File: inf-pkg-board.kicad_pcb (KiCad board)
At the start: 4 copper layers, 68.6 x 53.3 mm, 60 parts, among them J1 stemmaQT, J2 Conn_01x01_Pin, J3 Conn_01x01_Pin, J4 SWD, J5 USB_C_Receptacle_USB2.0_14P, J6 ePaper Hat, Q1 2N7002, U1 ME6211C33M5, U2 W25Q128JVS, U3 RP2040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

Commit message: fixes
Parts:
- removed U1: ME6211C33M5, Package_TO_SOT_SMD:SOT-23-5
- added C22: 100n, Capacitor_SMD:C_0402_1005Metric, F.Cu at (118.4, 96.3)
- added C23: 100p, Capacitor_SMD:C_0402_1005Metric, F.Cu at (83.8, 105.2)
- added C24: 100p, Capacitor_SMD:C_0402_1005Metric, F.Cu at (77.4, 98.8)
- added D2: LED, Diode_SMD:D_0805_2012Metric, F.Cu at (93.9, 97.8)
- added D3: LED, Diode_SMD:D_0805_2012Metric, F.Cu at (97.5, 99.6)
- added G***: LOGO, Symbol:infinity-small, F.Cu at (94.2, 117.9)
- added J7: Conn_01x01_Pin, Connector_PinHeader_1.00mm:PinHeader_1x01_P1.00mm_Vertical, F.Cu at (82.0, 112.0)
- added J8: Conn_01x01_Pin, Connector_PinHeader_1.00mm:PinHeader_1x01_P1.00mm_Vertical, F.Cu at (82.0, 109.0)
- added JP4: Jumper_2_Small_Bridged, Jumper:SolderJumper-2_P1.3mm_Bridged_Pad1.0x1.5mm, F.Cu at (138.0, 82.3)
- added Q2: AO3400A, Package_TO_SOT_SMD:SOT-23, F.Cu at (126.7, 112.6)
- added R14: 330, Resistor_SMD:R_0402_1005Metric, F.Cu at (136.4, 102.1)
- added R15: 5.1k, Resistor_SMD:R_0402_1005Metric, F.Cu at (85.6, 98.3)
- added R16: 330, Resistor_SMD:R_0402_1005Metric, F.Cu at (94.7, 99.3)
- added R17: 330, Resistor_SMD:R_0402_1005Metric, F.Cu at (92.1, 99.8)
- added R2: 27, Resistor_SMD:R_0402_1005Metric, F.Cu at (111.3, 120.7)
- added REF**: OSHW-Symbol_6.7x6mm_SilkScreen, Symbol:OSHW-Symbol_6.7x6mm_SilkScreen, F.Cu at (131.4, 82.3)
- added U7: SPX3819M5-L-3-3, Package_TO_SOT_SMD:SOT-23-5, F.Cu at (120.8, 98.7)
- L1: footprint Inductor_SMD:L_0201_0603Metric -> Inductor_SMD:L_0402_1005Metric
- Q1: value 2N7002 -> AO3400A
- R1, R13, R5, R6: footprint Capacitor_SMD:C_0402_1005Metric -> Resistor_SMD:R_0402_1005Metric
- R12: value 10k -> 1M; footprint Resistor_SMD:R_0805_2012Metric -> Resistor_SMD:R_0402_1005Metric
- R4: footprint Resistor_SMD:R_0402_1005Metric -> Resistor_SMD:R_0805_2012Metric
- moved C21 42.3 mm to (119.6, 101.9), turned to 90 degrees
- moved R12 24.7 mm to (116.1, 116.4), turned to -90 degrees
- moved R4 6.28 mm to (113.2, 101.2), turned to 90 degrees
- moved J3 2.55 mm to (85.9, 104.9)
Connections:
- C20 pad 2: Net-(U4-VBACKUP) -> Net-(Q2-G)
- R12 pad 1: Net-(D1-K) -> Net-(Q2-G)
- R12 pad 2: GND -> Net-(Q2-S)
- U3 pad 13: unconnected-(U3-GPIO10-Pad13) -> Net-(D2-A)
- U3 pad 14: unconnected-(U3-GPIO11-Pad14) -> Net-(D3-A)
- U3 pad 17: unconnected-(U3-GPIO14-Pad17) -> Net-(J8-Pin_1)
- U3 pad 18: unconnected-(U3-GPIO15-Pad18) -> Net-(J7-Pin_1)
- U4 pad 1: /32kHz -> Net-(U4-CLKOUT)
- U4 pad 2: /CC_GND -> Net-(Q2-S)
- U4 pad 6: Net-(U4-VBACKUP) -> Net-(Q2-G)
- U5 pad 2: Net-(J3-Pin_1) -> Net-(U5-FMI)
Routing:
- net Net-(Q2-G): track 0.00 -> 40.8 mm, vias 0 -> 3
- net Net-(U4-VBACKUP): track 35.1 -> 0.00 mm, vias 3 -> 0
- net Net-(J8-Pin_1): track 0.00 -> 30.4 mm, vias 0 -> 2
- net Net-(J7-Pin_1): track 0.00 -> 29.9 mm, vias 0 -> 2
- net GND: track 84.3 -> 101.8 mm, vias 38 -> 42
- net Net-(Q2-S): track 0.00 -> 17.5 mm, vias 0 -> 2
- net /CC_GND: track 79.0 -> 70.1 mm, vias 5 -> 4
- net Net-(D2-A): track 0.00 -> 4.26 mm
- net Net-(U5-FMI): track 0.00 -> 3.63 mm
- net Net-(D3-A): track 0.00 -> 2.88 mm
- net Net-(U5-~{SEN}): track 3.88 -> 6.64 mm
- net +3V3: track 75.6 -> 78.3 mm
- net /INIT: track 49.9 -> 47.4 mm
- net /32kHz: track 55.9 -> 53.5 mm
- net /D/C: track 34.0 -> 31.7 mm
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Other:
- board text added: "cut me"

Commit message: fix bom error / add debug pads
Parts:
- added J9: Conn_ARM_SWD_TagConnect_TC2030, Connector:Tag-Connect_TC2030-IDC-FP_2x03_P1.27mm_Vertical, F.Cu at (115.5, 90.9)
- added TP_CC_LATCH1: TestPoint, TestPoint:TestPoint_Pad_D1.5mm, F.Cu at (116.7, 80.3)
- added TP_CLK1: TestPoint, TestPoint:TestPoint_Pad_D1.5mm, F.Cu at (106.9, 116.0)
- added TP_GND1: TestPoint, TestPoint:TestPoint_Pad_D1.5mm, F.Cu at (130.8, 120.8)
- added TP_INT1: TestPoint, TestPoint:TestPoint_Pad_D1.5mm, F.Cu at (113.9, 122.8)
- added TP_V33: 3.3V_TEST, TestPoint:TestPoint_Pad_D2.0mm, F.Cu at (118.5, 121.3)
- added TP_VB1: VBUS_TEST, TestPoint:TestPoint_Pad_D2.0mm, F.Cu at (140.3, 87.1)
- J4: footprint Connector_PinHeader_1.27mm:PinHeader_2x05_P1.27mm_Vertical -> Connector_PinHeader_1.27mm:PinHeader_2x05_P1.27mm_Vertical_SMD
- R3: footprint Capacitor_SMD:C_0402_1005Metric -> Resistor_SMD:R_0402_1005Metric
- moved J4 27.3 mm to (137.9, 80.9)
- moved JP4 7.99 mm to (133.2, 75.9)
- moved REF** 1.80 mm to (130.1, 81.1)
- moved C10 1.42 mm to (106.2, 88.8)
- moved G*** 0.87 mm to (93.4, 117.6)
- moved C8 0.62 mm to (105.2, 88.0)
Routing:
- net /SWD: track 12.8 -> 50.7 mm, vias 0 -> 2
- net /SWCLK: track 17.6 -> 51.5 mm, vias 2 -> 6
- net /RUN: track 58.0 -> 85.7 mm, vias 3 -> 6
- net GND: track 101.8 -> 121.8 mm, vias 42 -> 45
- net +3V3: track 78.3 -> 94.5 mm, vias 12 -> 15
- net VBUS: track 35.9 -> 48.2 mm
- net /CC_GND: track 70.1 -> 63.7 mm
- net Net-(Q2-S): track 17.5 -> 23.0 mm
- net /32kHz: track 53.5 -> 58.6 mm
- net Net-(Q1-G): track 30.2 -> 31.9 mm
- net +1V1: track 29.0 -> 28.4 mm
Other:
- board text added: "return to sender"
- board text added: "rev2"

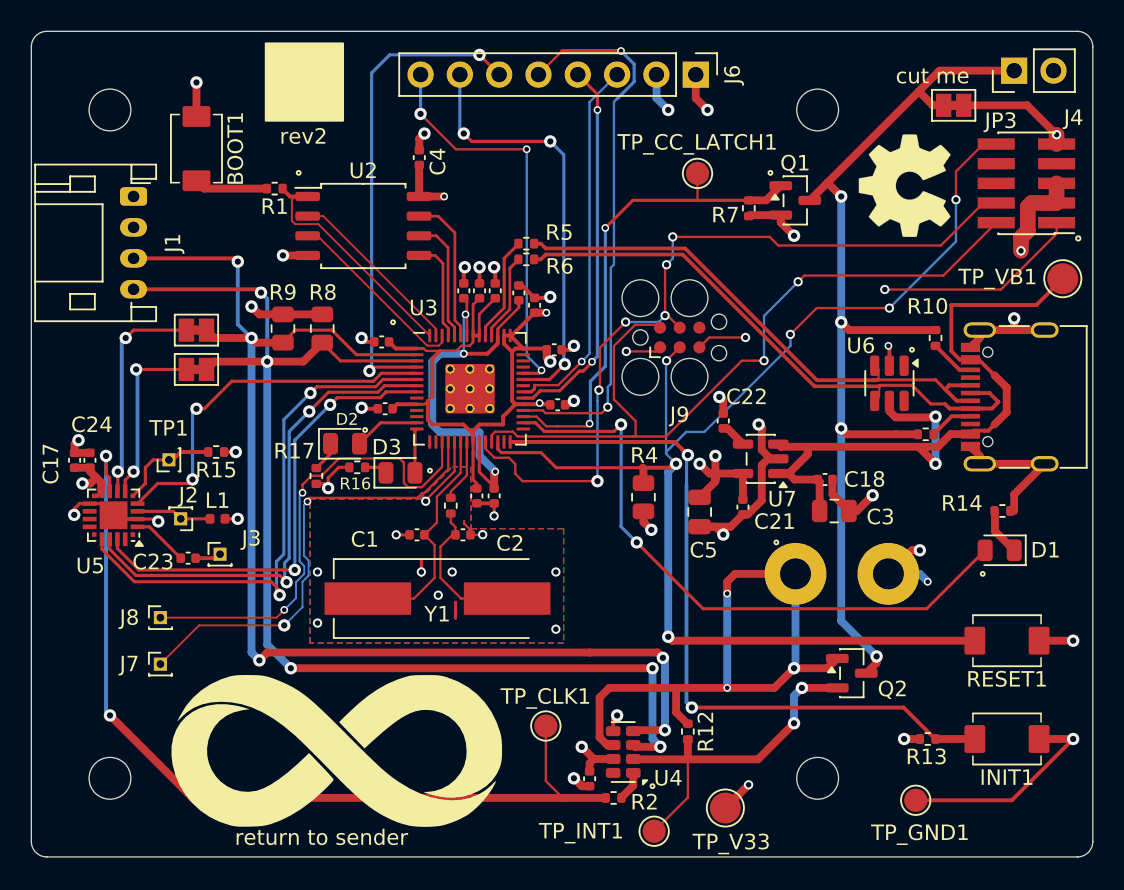
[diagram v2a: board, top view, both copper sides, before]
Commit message: bom optimization
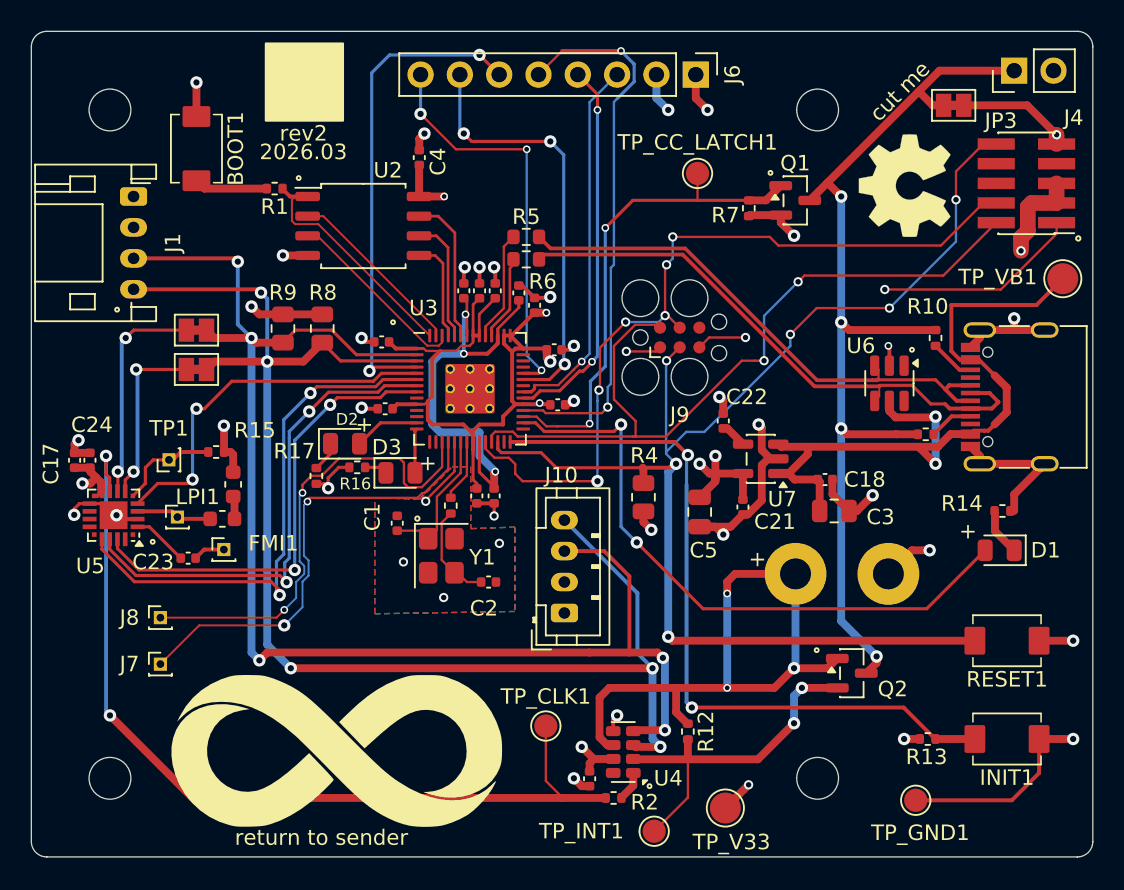
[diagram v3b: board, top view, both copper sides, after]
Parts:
- removed J2, J3: Conn_01x01_Pin, Connector_PinHeader_1.00mm:PinHeader_1x01_P1.00mm_Vertical
- added FMI1: Conn_01x01_Pin, Connector_PinHeader_1.00mm:PinHeader_1x01_P1.00mm_Vertical, F.Cu at (86.1, 104.6)
- added J10: stemmaQT, Connector_JST:JST_PH_B4B-PH-K_1x04_P2.00mm_Vertical, F.Cu at (108.1, 108.7)
- added L2: 68nH, Inductor_SMD:L_0603_1608Metric, F.Cu at (86.7, 100.4)
- added LPI1: Conn_01x01_Pin, Connector_PinHeader_1.00mm:PinHeader_1x01_P1.00mm_Vertical, F.Cu at (83.1, 102.5)
- C1, C2: value 27p -> 33p
- L1: value 120nH -> 68nH; footprint Inductor_SMD:L_0402_1005Metric -> Inductor_SMD:L_0603_1608Metric
- R5, R6: footprint Resistor_SMD:R_0402_1005Metric -> Resistor_SMD:R_0603_1608Metric
- Y1: value ABLS-12.000MHZ-B4-T -> Crystal_GND2; footprint RP2040_minimal:Crystal_SMD_HC49-US -> Crystal:Crystal_SMD_3225-4Pin_3.2x2.5mm
- moved C2 3.47 mm to (103.2, 106.7)
- moved Y1 2.78 mm to (100.2, 105.0), turned to -90 degrees
- moved C1 1.48 mm to (97.3, 102.9), turned to 90 degrees
- moved R5 0.44 mm to (105.6, 84.4)
- moved L1 0.31 mm to (86.0, 102.6)
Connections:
- L1 pad 2: GND -> Net-(L1-Pad2)
- Y1 pad 2: Net-(C2-Pad1) -> GND
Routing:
- net /SCL: track 78.6 -> 90.6 mm
- net /SDA: track 81.3 -> 91.1 mm
- net GND: track 121.8 -> 114.6 mm, vias 45 -> 37
- net /XIN: track 14.9 -> 9.34 mm
- net Net-(C2-Pad1): track 9.69 -> 6.38 mm
- net Net-(L1-Pad2): track 0.00 -> 1.48 mm
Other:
- board text added: "+"
- board text added: "2026.03"

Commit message: more ground
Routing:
- net +3V3: track 94.3 -> 97.3 mm, vias 15 -> 18
- net GND: track 114.6 -> 117.6 mm, vias 37 -> 39
- net +1V1: track 28.4 -> 27.4 mm
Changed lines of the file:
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@@
 		(tags "capacitor")
 		(property "Reference" "C2"
-			(at -0.3 1.7 0)
+			(at 0 1.3 0)
 			(layer "F.SilkS")
 			(effects
@@
 		(tags "capacitor")
 		(property "Reference" "C1"
-			(at 0.4 -1.6 90)
+			(at 0.4 -1.6 180)
 			(layer "F.SilkS")
 			(effects
@@
 		(tags "Through hole pin header THT 1x01 1.00mm single row")
 		(property "Reference" "LPI1"
-			(at 1.3 -1.3 0)
+			(at 0.2 -1.6 0)
 			(layer "F.SilkS")
 			(effects
@@
 	)
 	(segment
+		(start 101.6 87.404)
+		(end 103.632 87.404)
+		(width 0.254)
+		(layer "F.Cu")
+		(net 1)
+	)
+	(segment
 		(start 138.77 119.04)
 		(end 138.77 116.84)
@@
 	)
 	(segment
+		(start 102.441 102.341)
+		(end 102.6 102.5)
+		(width 0.2032)
+		(layer "F.Cu")
+		(net 1)
+	)
+	(segment
 		(start 105.156 87.54)
 		(end 105.372 87.54)
@@
 	)
 	(segment
+		(start 102.441 101.615)
+		(end 102.441 102.341)
+		(width 0.2032)
+		(layer "F.Cu")
+		(net 1)
+	)
+	(segment
 		(start 116.84 103.124)
 		(end 118.844 103.124)
@@
 	)
 	(via
+		(at 96 103.6)
+		(size 0.8)
+		(drill 0.4)
+		(layers "F.Cu" "B.Cu")
+		(free yes)
+		(net 1)
+	)
+	(via
 		(at 128.016 101.092)
 		(size 0.8)
@@
 	)
 	(via
+		(at 102.6 102.5)
+		(size 0.8)
+		(drill 0.4)
+		(layers "F.Cu" "B.Cu")
+		(net 1)
+	)
+	(via
 		(at 101.665 86.36)
 		(size 0.8)
@@
 	)
 	(segment
+		(start 96.774 91.186)
+		(end 96.774 90.574)
+		(width 0.254)
+		(layer "F.Cu")
+		(net 5)
+	)
+	(segment
 		(start 104.2 91.303252)
 		(end 104.722 91.825252)
@@
 	)
 	(segment
+		(start 102.199 100.0945)
+		(end 102.199 99.7)
+		(width 0.2)
+		(layer "F.Cu")
+		(net 5)
+	)
+	(segment
 		(start 101.572748 96.52)
 		(end 102.094374 97.041626)
@@
 	)
 	(segment
+		(start 103.30613 89.00613)
+		(end 103.25813 89.00613)
+		(width 0.254)
+		(layer "F.Cu")
+		(net 5)
+	)
+	(segment
+		(start 103.00613 89.00613)
+		(end 103.30613 89.00613)
+		(width 0.254)
+		(layer "F.Cu")
+		(net 5)
+	)
+	(segment
 		(start 99.06 95.2125)
 		(end 99.2765 94.996)
@@
 	)
 	(segment
+		(start 102.6 89.396)
+		(end 102.998 88.998)
+		(width 0.1778)
+		(layer "F.Cu")
+		(net 5)
+	)
+	(segment
 		(start 78.169 100.267)
 		(end 78.169 100.832)
@@
 	)
 	(segment
-		(start 102.199 100.0945)
+		(start 102.199 99.7)
 		(end 102.199 98.4)
 		(width 0.2)
@@
 	)
 	(segment
+		(start 102.199 99.7)
+		(end 102.6 99.7)
+		(width 0.254)
+		(layer "F.Cu")
+		(net 5)
+	)
+	(segment
 		(start 102.6 90.775)
 		(end 102.6 89.396)
@@
 	)
 	(segment
+		(start 102.441 100.3365)
+		(end 102.441 100.655)
+		(width 0.2032)
+		(layer "F.Cu")
+		(net 5)
+	)
+	(segment
 		(start 98.71 81.79)
 		(end 98.71 79.771)
@@
 	)
 	(segment
+		(start 103.25813 89.00613)
+		(end 102.616 88.364)
+		(width 0.254)
+		(layer "F.Cu")
+		(net 5)
+	)
+	(segment
 		(start 106.962 92.23)
 		(end 107.188 92.456)
@@
 	)
 	(segment
+		(start 102.998 88.998)
+		(end 103.00613 89.00613)
+		(width 0.254)
+		(layer "F.Cu")
+		(net 5)
+	)
+	(segment
 		(start 97.2005 91.6125)
 		(end 96.774 91.186)
@@
 	)
 	(segment
+		(start 96.774 90.574)
+		(end 96.5 90.3)
+		(width 0.254)
+		(layer "F.Cu")
+		(net 5)
+	)
+	(segment
 		(start 106.6137 95.25)
 		(end 106.5 95.1363)
@@
 	)
 	(segment
-		(start 102.6 89.396)
+		(start 102.998 88.998)
 		(end 103.632 88.364)
 		(width 0.1778)
@@
 	)
 	(via
+		(at 103.30613 89.00613)
+		(size 0.8)
+		(drill 0.4)
+		(layers "F.Cu" "B.Cu")
+		(net 5)
+	)
+	(via
 		(at 109.22 117.348)
 		(size 0.8)
@@
 	)
 	(via
+		(at 102.6 99.7)
+		(size 0.8)
+		(drill 0.4)
+		(layers "F.Cu" "B.Cu")
+		(net 5)
+	)
+	(via
 		(at 112.1 91.8)
 		(size 0.6)
@@
 	)
 	(via
+		(at 96.5 90.3)
+		(size 0.8)
+		(drill 0.4)
+		(layers "F.Cu" "B.Cu")
+		(net 5)
+	)
+	(via
 		(at 120 119.8)
 		(size 0.6)
@@
 	)
 	(segment
-		(start 101.8 88.564)
-		(end 101.8 90.775)
-		(width 0.1778)
+		(start 102.6 98.536)
+		(end 103.632 99.568)
+		(width 0.2032)
 		(layer "F.Cu")
 		(net 6)
 	)
 	(segment
-		(start 102.6 99.59)
-		(end 102.6 97.65)
-		(width 0.2)
-		(locked yes)
+		(start 101.8 88.564)
+		(end 101.8 90.775)
+		(width 0.1778)
 		(layer "F.Cu")
 		(net 6)
@@
 	)
 	(segment
-		(start 103.56 100.55)
-		(end 102.6 99.59)
-		(width 0.2)
-		(locked yes)
-		(layer "F.Cu")
-		(net 6)
-	)
-	(segment
 		(start 103.129748 91.948)
 		(end 103.795 91.282748)
@@
 	)
 	(segment
+		(start 102.6 97.65)
+		(end 102.6 98.536)
+		(width 0.2032)
+		(layer "F.Cu")
+		(net 6)
+	)
+	(segment
 		(start 105.156 88.5)
 		(end 105.156 88.952171)
@@
 		(polygon
 			(pts
-				(xy 104.9 103.15) (xy 104.9 108.6) (xy 95.85 108.75) (xy 95.85 101.25) (xy 98.75 101.35) (xy 100.85 99.25)
+				(xy 104.9 103.15) (xy 104.9 108.6) (xy 95.45 108.75) (xy 95.45 101.25) (xy 98.75 101.35) (xy 100.85 99.25)
 				(xy 102.05 99.25) (xy 102.05 103.25)
 			)

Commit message: final tweaks
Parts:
- added R18: 0, Resistor_SMD:R_1206_3216Metric_Pad1.30x1.75mm_HandSolder, F.Cu at (120.0, 110.8)
- J10: value stemmaQT -> stemma
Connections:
- C20 pad 2: Net-(Q2-G) -> Net-(C20-Pad2)
- U4 pad 8: unconnected-(U4-EVI-Pad8) -> GND
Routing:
- net Net-(Q2-G): track 40.8 -> 23.9 mm, vias 3 -> 0
- net Net-(C20-Pad2): track 0.00 -> 6.44 mm
- net /LED: track 40.6 -> 37.9 mm
- net GND: track 117.6 -> 119.5 mm
- net /RUN: track 85.7 -> 86.8 mm, vias 6 -> 8

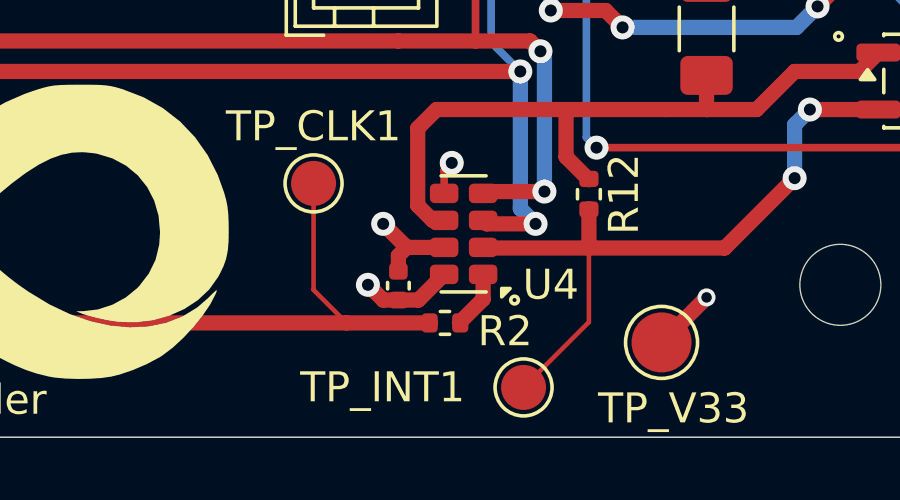
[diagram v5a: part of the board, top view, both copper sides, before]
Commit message: swap resistor to smaller/standard size
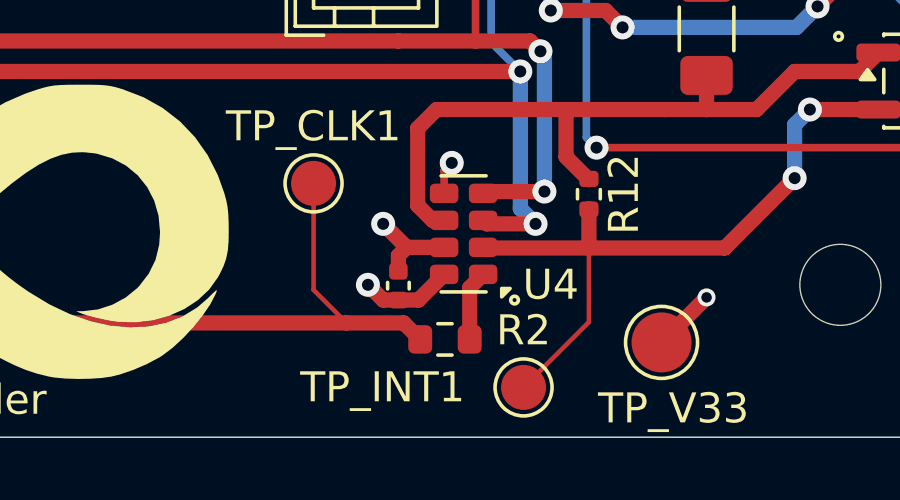
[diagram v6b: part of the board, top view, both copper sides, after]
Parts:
- R2: footprint Resistor_SMD:R_0402_1005Metric -> Resistor_SMD:R_0603_1608Metric
- moved R2 0.55 mm to (111.3, 121.2)
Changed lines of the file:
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@@
 		(embedded_fonts no)
 	)
-	(footprint "Resistor_SMD:R_0402_1005Metric"
+	(footprint "Resistor_SMD:R_0603_1608Metric"
 		(layer "F.Cu")
-		(at 111.28 120.65)
-		(descr "Resistor SMD 0402 (1005 Metric), square (rectangular) end terminal, IPC-7351 nominal, (Body size source: IPC-SM-782 page 72, https://www.pcb-3d.com/wordpress/wp-content/uploads/ipc-sm-782a_amendment_1_and_2.pdf), generated with kicad-footprint-generator")
+		(at 111.28 121.2)
+		(descr "Resistor SMD 0603 (1608 Metric), square (rectangular) end terminal, IPC-7351 nominal, (Body size source: IPC-SM-782 page 72, https://www.pcb-3d.com/wordpress/wp-content/uploads/ipc-sm-782a_amendment_1_and_2.pdf), generated with kicad-footprint-generator")
 		(tags "resistor")
 		(property "Reference" "R2"
-			(at 2.004 0.2794 0)
+			(at 2.62 -0.3 0)
 			(layer "F.SilkS")
 			(effects
@@
 		)
 		(property "Value" "27"
-			(at 0 1.17 0)
+			(at 0 1.43 0)
 			(layer "F.Fab")
-			(hide yes)
 			(effects
 				(font
@@
 			)
 		)
-		(property "LCSC" "C274349"
+		(property "LCSC" "C25190"
 			(at 0 0 0)
 			(unlocked yes)
@@
 		(attr smd)
 		(fp_line
-			(start -0.153641 -0.38)
-			(end 0.153641 -0.38)
+			(start -0.237258 -0.5225)
+			(end 0.237258 -0.5225)
 			(stroke
 				(width 0.12)
@@
 		)
 		(fp_line
-			(start -0.153641 0.38)
-			(end 0.153641 0.38)
+			(start -0.237258 0.5225)
+			(end 0.237258 0.5225)
 			(stroke
 				(width 0.12)
@@
 		)
 		(fp_rect
-			(start -0.93 -0.47)
-			(end 0.93 0.47)
+			(start -1.48 -0.73)
+			(end 1.48 0.73)
 			(stroke
 				(width 0.05)
@@
 		)
 		(fp_rect
-			(start -0.525 -0.27)
-			(end 0.525 0.27)
+			(start -0.8 -0.4125)
+			(end 0.8 0.4125)
 			(stroke
 				(width 0.1)
@@
 			(effects
 				(font
-					(size 0.26 0.26)
-					(thickness 0.04)
+					(size 0.4 0.4)
+					(thickness 0.06)
 				)
 			)
 		)
 		(pad "1" smd roundrect
-			(at -0.51 0)
-			(size 0.54 0.64)
+			(at -0.825 0)
+			(size 0.8 0.95)
 			(layers "F.Cu" "F.Mask" "F.Paste")
 			(roundrect_rratio 0.25)
@@
 		)
 		(pad "2" smd roundrect
-			(at 0.51 0)
-			(size 0.54 0.64)
+			(at 0.825 0)
+			(size 0.8 0.95)
 			(layers "F.Cu" "F.Mask" "F.Paste")
 			(roundrect_rratio 0.25)
@@
 		)
 		(embedded_fonts no)
-		(model "${KICAD9_3DMODEL_DIR}/Resistor_SMD.3dshapes/R_0402_1005Metric.step"
+		(model "${KICAD9_3DMODEL_DIR}/Resistor_SMD.3dshapes/R_0603_1608Metric.step"
 			(offset
 				(xyz 0 0 0)
@@
 	)
 	(segment
+		(start 109.905 120.65)
+		(end 110.455 121.2)
+		(width 0.508)
+		(layer "F.Cu")
+		(net 53)
+	)
+	(segment
 		(start 78.486 99.728916)
 		(end 78.486 98.552)
@@
 	)
 	(segment
-		(start 110.8 120.65)
-		(end 108 120.65)
+		(start 108 120.65)
+		(end 109.905 120.65)
 		(width 0.508)
 		(layer "F.Cu")
@@
 	)
 	(segment
-		(start 112.552 119.032)
-		(end 112.552 119.858)
+		(start 112.105 121.2)
+		(end 112.105 119.479)
 		(width 0.508)
 		(layer "F.Cu")
@@
 	)
 	(segment
-		(start 112.552 119.858)
-		(end 111.76 120.65)
+		(start 112.105 119.479)
+		(end 112.552 119.032)
 		(width 0.508)
 		(layer "F.Cu")
